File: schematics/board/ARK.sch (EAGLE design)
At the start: 207 parts, among them IC2 STM32F103C8T, Q5 8MHz

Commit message: Резисторы у FS8205A 100Ом
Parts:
- R88, R89, R90, R91, R92, R93, R94, R95, R96, R97, R98, R99: value 10k -> 100R
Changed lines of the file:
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@@
 <part name="R62" library="resistor" library_urn="urn:adsk.eagle:library:348" deviceset="R-US_" device="R0603" package3d_urn="urn:adsk.eagle:package:23555/3" value="232k"/>
 <part name="R87" library="resistor" library_urn="urn:adsk.eagle:library:348" deviceset="R-US_" device="R0603" package3d_urn="urn:adsk.eagle:package:23555/3" value="680k"/>
-<part name="R88" library="resistor" library_urn="urn:adsk.eagle:library:348" deviceset="R-US_" device="R0603" package3d_urn="urn:adsk.eagle:package:23555/3" value="10k"/>
-<part name="R89" library="resistor" library_urn="urn:adsk.eagle:library:348" deviceset="R-US_" device="R0603" package3d_urn="urn:adsk.eagle:package:23555/3" value="10k"/>
-<part name="R90" library="resistor" library_urn="urn:adsk.eagle:library:348" deviceset="R-US_" device="R0603" package3d_urn="urn:adsk.eagle:package:23555/3" value="10k"/>
-<part name="R91" library="resistor" library_urn="urn:adsk.eagle:library:348" deviceset="R-US_" device="R0603" package3d_urn="urn:adsk.eagle:package:23555/3" value="10k"/>
-<part name="R92" library="resistor" library_urn="urn:adsk.eagle:library:348" deviceset="R-US_" device="R0603" package3d_urn="urn:adsk.eagle:package:23555/3" value="10k"/>
-<part name="R93" library="resistor" library_urn="urn:adsk.eagle:library:348" deviceset="R-US_" device="R0603" package3d_urn="urn:adsk.eagle:package:23555/3" value="10k"/>
-<part name="R94" library="resistor" library_urn="urn:adsk.eagle:library:348" deviceset="R-US_" device="R0603" package3d_urn="urn:adsk.eagle:package:23555/3" value="10k"/>
-<part name="R95" library="resistor" library_urn="urn:adsk.eagle:library:348" deviceset="R-US_" device="R0603" package3d_urn="urn:adsk.eagle:package:23555/3" value="10k"/>
-<part name="R96" library="resistor" library_urn="urn:adsk.eagle:library:348" deviceset="R-US_" device="R0603" package3d_urn="urn:adsk.eagle:package:23555/3" value="10k"/>
-<part name="R97" library="resistor" library_urn="urn:adsk.eagle:library:348" deviceset="R-US_" device="R0603" package3d_urn="urn:adsk.eagle:package:23555/3" value="10k"/>
-<part name="R98" library="resistor" library_urn="urn:adsk.eagle:library:348" deviceset="R-US_" device="R0603" package3d_urn="urn:adsk.eagle:package:23555/3" value="10k"/>
-<part name="R99" library="resistor" library_urn="urn:adsk.eagle:library:348" deviceset="R-US_" device="R0603" package3d_urn="urn:adsk.eagle:package:23555/3" value="10k"/>
+<part name="R88" library="resistor" library_urn="urn:adsk.eagle:library:348" deviceset="R-US_" device="R0603" package3d_urn="urn:adsk.eagle:package:23555/3" value="100R"/>
+<part name="R89" library="resistor" library_urn="urn:adsk.eagle:library:348" deviceset="R-US_" device="R0603" package3d_urn="urn:adsk.eagle:package:23555/3" value="100R"/>
+<part name="R90" library="resistor" library_urn="urn:adsk.eagle:library:348" deviceset="R-US_" device="R0603" package3d_urn="urn:adsk.eagle:package:23555/3" value="100R"/>
+<part name="R91" library="resistor" library_urn="urn:adsk.eagle:library:348" deviceset="R-US_" device="R0603" package3d_urn="urn:adsk.eagle:package:23555/3" value="100R"/>
+<part name="R92" library="resistor" library_urn="urn:adsk.eagle:library:348" deviceset="R-US_" device="R0603" package3d_urn="urn:adsk.eagle:package:23555/3" value="100R"/>
+<part name="R93" library="resistor" library_urn="urn:adsk.eagle:library:348" deviceset="R-US_" device="R0603" package3d_urn="urn:adsk.eagle:package:23555/3" value="100R"/>
+<part name="R94" library="resistor" library_urn="urn:adsk.eagle:library:348" deviceset="R-US_" device="R0603" package3d_urn="urn:adsk.eagle:package:23555/3" value="100R"/>
+<part name="R95" library="resistor" library_urn="urn:adsk.eagle:library:348" deviceset="R-US_" device="R0603" package3d_urn="urn:adsk.eagle:package:23555/3" value="100R"/>
+<part name="R96" library="resistor" library_urn="urn:adsk.eagle:library:348" deviceset="R-US_" device="R0603" package3d_urn="urn:adsk.eagle:package:23555/3" value="100R"/>
+<part name="R97" library="resistor" library_urn="urn:adsk.eagle:library:348" deviceset="R-US_" device="R0603" package3d_urn="urn:adsk.eagle:package:23555/3" value="100R"/>
+<part name="R98" library="resistor" library_urn="urn:adsk.eagle:library:348" deviceset="R-US_" device="R0603" package3d_urn="urn:adsk.eagle:package:23555/3" value="100R"/>
+<part name="R99" library="resistor" library_urn="urn:adsk.eagle:library:348" deviceset="R-US_" device="R0603" package3d_urn="urn:adsk.eagle:package:23555/3" value="100R"/>
 <part name="PWR" library="led" library_urn="urn:adsk.eagle:library:259" deviceset="LED" device="CHIPLED_0603" package3d_urn="urn:adsk.eagle:package:15822/2"/>
 <part name="PB5" library="led" library_urn="urn:adsk.eagle:library:259" deviceset="LED" device="CHIPLED_0603" package3d_urn="urn:adsk.eagle:package:15822/2"/>

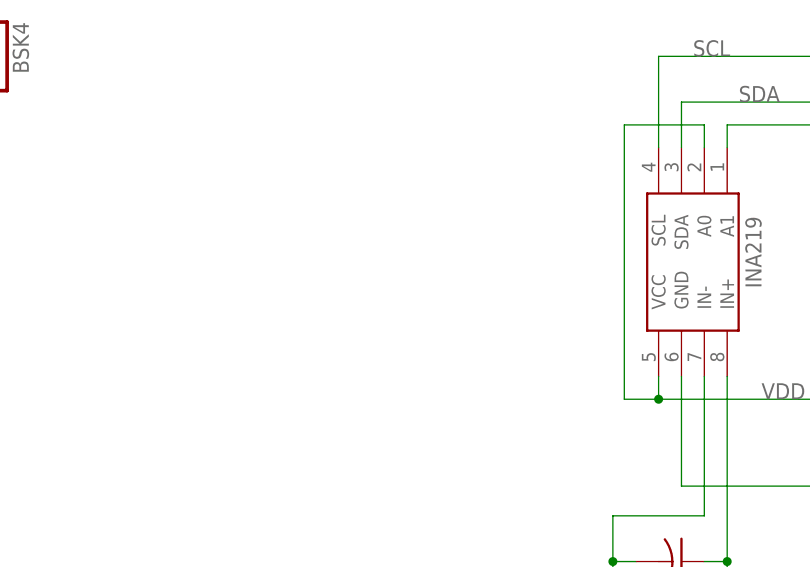
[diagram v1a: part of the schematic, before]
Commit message: Добавлен micro-USB на АРК
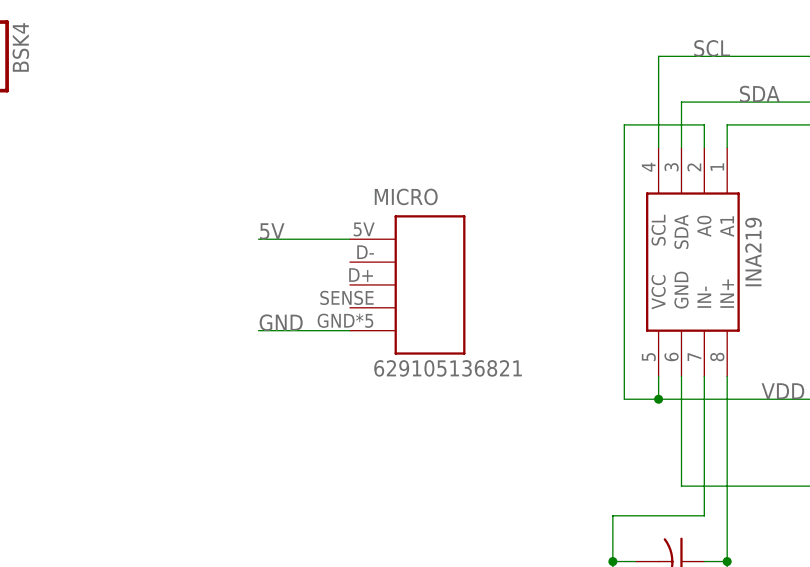
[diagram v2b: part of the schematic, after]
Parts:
- added MICRO: 629105136821, MicroUSB:629105136821
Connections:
- net 5V: now also MICRO.1
- net GND: now also MICRO.5
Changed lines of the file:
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@@
 <layer number="48" name="Document" color="7" fill="1" visible="no" active="no"/>
 <layer number="49" name="Reference" color="7" fill="1" visible="no" active="no"/>
+<layer number="50" name="dxf" color="7" fill="1" visible="no" active="no"/>
 <layer number="51" name="tDocu" color="7" fill="1" visible="no" active="no"/>
 <layer number="52" name="bDocu" color="7" fill="1" visible="no" active="no"/>
+<layer number="53" name="tGND_GNDA" color="7" fill="9" visible="no" active="no"/>
+<layer number="54" name="bGND_GNDA" color="1" fill="9" visible="no" active="no"/>
+<layer number="56" name="wert" color="7" fill="1" visible="no" active="no"/>
 <layer number="88" name="SimResults" color="9" fill="1" visible="yes" active="yes"/>
 <layer number="89" name="SimProbes" color="9" fill="1" visible="yes" active="yes"/>
@@
 <layer number="101" name="NotChangedData" color="15" fill="1" visible="yes" active="yes"/>
 <layer number="102" name="ChangedData" color="15" fill="1" visible="yes" active="yes"/>
+<layer number="103" name="tMap" color="7" fill="1" visible="no" active="no"/>
+<layer number="104" name="Name" color="7" fill="1" visible="no" active="no"/>
+<layer number="105" name="tPlate" color="7" fill="1" visible="no" active="no"/>
+<layer number="106" name="bPlate" color="7" fill="1" visible="no" active="no"/>
+<layer number="107" name="Crop" color="7" fill="1" visible="no" active="no"/>
+<layer number="108" name="fp8" color="7" fill="1" visible="no" active="no"/>
+<layer number="109" name="fp9" color="7" fill="1" visible="no" active="no"/>
+<layer number="110" name="110" color="7" fill="1" visible="no" active="no"/>
+<layer number="111" name="111" color="7" fill="1" visible="no" active="no"/>
+<layer number="112" name="tSilk" color="7" fill="1" visible="no" active="no"/>
+<layer number="113" name="IDFDebug" color="7" fill="1" visible="no" active="yes"/>
+<layer number="116" name="Patch_BOT" color="9" fill="4" visible="no" active="no"/>
+<layer number="118" name="Rect_Pads" color="7" fill="1" visible="no" active="no"/>
+<layer number="121" name="_tsilk" color="7" fill="1" visible="no" active="no"/>
+<layer number="122" name="_bsilk" color="7" fill="1" visible="no" active="no"/>
+<layer number="123" name="tTestmark" color="7" fill="1" visible="no" active="no"/>
+<layer number="124" name="bTestmark" color="7" fill="1" visible="no" active="no"/>
+<layer number="125" name="_tNames" color="7" fill="1" visible="no" active="no"/>
+<layer number="126" name="_bNames" color="7" fill="1" visible="no" active="no"/>
+<layer number="127" name="_tValues" color="7" fill="1" visible="no" active="no"/>
+<layer number="128" name="_bValues" color="7" fill="1" visible="no" active="no"/>
+<layer number="131" name="tAdjust" color="7" fill="1" visible="no" active="no"/>
+<layer number="132" name="bAdjust" color="7" fill="1" visible="no" active="no"/>
+<layer number="144" name="DrillLegend" color="7" fill="1" visible="no" active="no"/>
+<layer number="151" name="HeatSink" color="14" fill="1" visible="no" active="no"/>
+<layer number="152" name="_bDocu" color="7" fill="1" visible="no" active="no"/>
+<layer number="199" name="Contour" color="7" fill="1" visible="no" active="no"/>
+<layer number="200" name="200bmp" color="1" fill="10" visible="no" active="no"/>
+<layer number="201" name="201bmp" color="2" fill="1" visible="no" active="no"/>
+<layer number="202" name="202bmp" color="3" fill="1" visible="no" active="no"/>
+<layer number="203" name="203bmp" color="4" fill="10" visible="no" active="no"/>
+<layer number="204" name="204bmp" color="5" fill="10" visible="no" active="no"/>
+<layer number="205" name="205bmp" color="6" fill="10" visible="no" active="no"/>
+<layer number="206" name="206bmp" color="7" fill="10" visible="no" active="no"/>
+<layer number="207" name="207bmp" color="15" fill="10" visible="no" active="no"/>
+<layer number="208" name="208bmp" color="9" fill="10" visible="no" active="no"/>
+<layer number="209" name="209bmp" color="7" fill="1" visible="no" active="no"/>
+<layer number="210" name="210bmp" color="7" fill="1" visible="no" active="no"/>
+<layer number="211" name="211bmp" color="7" fill="1" visible="no" active="no"/>
+<layer number="212" name="212bmp" color="7" fill="1" visible="no" active="no"/>
+<layer number="213" name="213bmp" color="7" fill="1" visible="no" active="no"/>
+<layer number="214" name="214bmp" color="7" fill="1" visible="no" active="no"/>
+<layer number="215" name="215bmp" color="7" fill="1" visible="no" active="no"/>
+<layer number="216" name="216bmp" color="7" fill="1" visible="no" active="no"/>
+<layer number="217" name="217bmp" color="18" fill="1" visible="no" active="no"/>
+<layer number="218" name="218bmp" color="19" fill="1" visible="no" active="no"/>
+<layer number="219" name="219bmp" color="20" fill="1" visible="no" active="no"/>
+<layer number="220" name="220bmp" color="21" fill="1" visible="no" active="no"/>
+<layer number="221" name="221bmp" color="22" fill="1" visible="no" active="no"/>
+<layer number="222" name="222bmp" color="23" fill="1" visible="no" active="no"/>
+<layer number="223" name="223bmp" color="24" fill="1" visible="no" active="no"/>
+<layer number="224" name="224bmp" color="25" fill="1" visible="no" active="no"/>
+<layer number="225" name="225bmp" color="7" fill="1" visible="no" active="yes"/>
+<layer number="226" name="226bmp" color="7" fill="1" visible="no" active="yes"/>
+<layer number="227" name="227bmp" color="7" fill="1" visible="no" active="yes"/>
+<layer number="228" name="228bmp" color="7" fill="1" visible="no" active="yes"/>
+<layer number="230" name="230bmp" color="7" fill="1" visible="no" active="yes"/>
+<layer number="248" name="Housing" color="7" fill="1" visible="no" active="no"/>
+<layer number="249" name="Edge" color="7" fill="1" visible="no" active="no"/>
+<layer number="250" name="Descript" color="7" fill="1" visible="no" active="yes"/>
+<layer number="251" name="SMDround" color="7" fill="1" visible="no" active="yes"/>
+<layer number="254" name="OrgLBR" color="13" fill="1" visible="no" active="no"/>
 </layers>
 <schematic xreflabel="%F%N/%S.%C%R" xrefpart="/%S.%C%R">
@@
 <part name="R25" library="resistor" library_urn="urn:adsk.eagle:library:348" deviceset="R-US_" device="R0603" package3d_urn="urn:adsk.eagle:package:23555/3" value="5k1"/>
 <part name="R26" library="resistor" library_urn="urn:adsk.eagle:library:348" deviceset="R-US_" device="R0603" package3d_urn="urn:adsk.eagle:package:23555/3" value="5k1"/>
+<part name="MICRO" library="MicroUSB" deviceset="629105136821" device=""/>
 </parts>
 <sheets>
@@
 <attribute name="VALUE" x="534.162" y="290.83" size="1.778" layer="96" rot="R90"/>
 </instance>
+<instance part="MICRO" gate="G$1" x="515.62" y="231.14" smashed="yes">
+<attribute name="NAME" x="508" y="245.11" size="1.778" layer="95"/>
+<attribute name="VALUE" x="508" y="226.06" size="1.778" layer="96"/>
+</instance>
 </instances>
 <busses>
@@
 <label x="513.08" y="312.42" size="1.778" layer="95" rot="R90"/>
 </segment>
+<segment>
+<pinref part="MICRO" gate="G$1" pin="5"/>
+<wire x1="505.46" y1="231.14" x2="495.3" y2="231.14" width="0.1524" layer="91"/>
+<label x="495.3" y="231.14" size="1.778" layer="95"/>
+</segment>
 </net>
 <net name="INA_BUS+" class="0">
@@
 <pinref part="BSK4" gate="A" pin="8"/>
 </segment>
+<segment>
+<pinref part="MICRO" gate="G$1" pin="1"/>
+<wire x1="505.46" y1="241.3" x2="495.3" y2="241.3" width="0.1524" layer="91"/>
+<label x="495.3" y="241.3" size="1.778" layer="95"/>
+</segment>
 </net>

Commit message: Изменения в подключении мк
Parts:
- added C15, C53, C54, C55: 100nF, rcl:C-EUC0603
- added C16: 10µ, rcl:C-USC1206
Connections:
- net GND: now also C15.2, C16.2, C53.2, C54.2, C55.2
- net VDD: now also C15.1, C16.1, C53.1, C54.1, C55.1, IC2.VBAT
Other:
- moved on the sheet: R79
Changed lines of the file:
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@@
 <part name="R26" library="resistor" library_urn="urn:adsk.eagle:library:348" deviceset="R-US_" device="R0603" package3d_urn="urn:adsk.eagle:package:23555/3" value="5k1"/>
 <part name="MICRO" library="MicroUSB" deviceset="629105136821" device=""/>
+<part name="C15" library="rcl" library_urn="urn:adsk.eagle:library:334" deviceset="C-EU" device="C0603" package3d_urn="urn:adsk.eagle:package:23616/2" value="100nF"/>
+<part name="C16" library="rcl" library_urn="urn:adsk.eagle:library:334" deviceset="C-US" device="C1206" package3d_urn="urn:adsk.eagle:package:23618/2" value="10µ"/>
+<part name="C53" library="rcl" library_urn="urn:adsk.eagle:library:334" deviceset="C-EU" device="C0603" package3d_urn="urn:adsk.eagle:package:23616/2" value="100nF"/>
+<part name="C54" library="rcl" library_urn="urn:adsk.eagle:library:334" deviceset="C-EU" device="C0603" package3d_urn="urn:adsk.eagle:package:23616/2" value="100nF"/>
+<part name="C55" library="rcl" library_urn="urn:adsk.eagle:library:334" deviceset="C-EU" device="C0603" package3d_urn="urn:adsk.eagle:package:23616/2" value="100nF"/>
 </parts>
 <sheets>
@@
 <instance part="U$26" gate="G$1" x="58.42" y="43.18" smashed="yes"/>
 <instance part="U$1" gate="G$1" x="241.3" y="50.8" smashed="yes"/>
-<instance part="R79" gate="G$1" x="462.28" y="378.46" smashed="yes">
-<attribute name="NAME" x="458.47" y="379.9586" size="1.778" layer="95"/>
-<attribute name="VALUE" x="458.47" y="375.158" size="1.778" layer="96"/>
+<instance part="R79" gate="G$1" x="441.96" y="375.92" smashed="yes">
+<attribute name="NAME" x="438.15" y="377.4186" size="1.778" layer="95"/>
+<attribute name="VALUE" x="438.15" y="372.618" size="1.778" layer="96"/>
 </instance>
 <instance part="LED3" gate="G$1" x="297.18" y="292.1" smashed="yes" rot="R270">
@@
 <attribute name="VALUE" x="508" y="226.06" size="1.778" layer="96"/>
 </instance>
+<instance part="C15" gate="G$1" x="472.44" y="383.54" smashed="yes" rot="R270">
+<attribute name="NAME" x="472.821" y="382.016" size="1.778" layer="95" rot="R270"/>
+<attribute name="VALUE" x="467.741" y="382.016" size="1.778" layer="96" rot="R270"/>
+</instance>
+<instance part="C16" gate="G$1" x="472.44" y="388.62" smashed="yes" rot="R270">
+<attribute name="NAME" x="473.075" y="387.604" size="1.778" layer="95" rot="R270"/>
+<attribute name="VALUE" x="468.249" y="387.604" size="1.778" layer="96" rot="R270"/>
+</instance>
+<instance part="C53" gate="G$1" x="472.44" y="396.24" smashed="yes" rot="R270">
+<attribute name="NAME" x="472.821" y="394.716" size="1.778" layer="95" rot="R270"/>
+<attribute name="VALUE" x="467.741" y="394.716" size="1.778" layer="96" rot="R270"/>
+</instance>
+<instance part="C54" gate="G$1" x="472.44" y="403.86" smashed="yes" rot="R270">
+<attribute name="NAME" x="472.821" y="402.336" size="1.778" layer="95" rot="R270"/>
+<attribute name="VALUE" x="467.741" y="402.336" size="1.778" layer="96" rot="R270"/>
+</instance>
+<instance part="C55" gate="G$1" x="472.44" y="411.48" smashed="yes" rot="R270">
+<attribute name="NAME" x="472.821" y="409.956" size="1.778" layer="95" rot="R270"/>
+<attribute name="VALUE" x="467.741" y="409.956" size="1.778" layer="96" rot="R270"/>
+</instance>
 </instances>
 <busses>
@@
 </segment>
 <segment>
-<wire x1="472.44" y1="368.3" x2="472.44" y2="375.92" width="0.1524" layer="91"/>
-<label x="472.44" y="370.84" size="1.778" layer="95" rot="R90"/>
+<wire x1="472.44" y1="368.3" x2="472.44" y2="378.46" width="0.1524" layer="91"/>
+<label x="467.36" y="424.18" size="1.778" layer="95" rot="R90"/>
 <pinref part="IC2" gate="MCU" pin="VSSA"/>
+<wire x1="472.44" y1="378.46" x2="467.36" y2="378.46" width="0.1524" layer="91"/>
+<wire x1="467.36" y1="378.46" x2="467.36" y2="383.54" width="0.1524" layer="91"/>
+<pinref part="C15" gate="G$1" pin="2"/>
+<wire x1="467.36" y1="383.54" x2="467.36" y2="388.62" width="0.1524" layer="91"/>
+<junction x="467.36" y="383.54"/>
+<pinref part="C16" gate="G$1" pin="2"/>
+<wire x1="467.36" y1="388.62" x2="467.36" y2="396.24" width="0.1524" layer="91"/>
+<junction x="467.36" y="388.62"/>
+<pinref part="C53" gate="G$1" pin="2"/>
+<wire x1="467.36" y1="396.24" x2="467.36" y2="403.86" width="0.1524" layer="91"/>
+<junction x="467.36" y="396.24"/>
+<pinref part="C54" gate="G$1" pin="2"/>
+<wire x1="467.36" y1="403.86" x2="467.36" y2="411.48" width="0.1524" layer="91"/>
+<junction x="467.36" y="403.86"/>
+<pinref part="C55" gate="G$1" pin="2"/>
+<wire x1="467.36" y1="411.48" x2="467.36" y2="429.26" width="0.1524" layer="91"/>
+<junction x="467.36" y="411.48"/>
 </segment>
 <segment>
@@
 </segment>
 <segment>
-<wire x1="474.98" y1="368.3" x2="474.98" y2="375.92" width="0.1524" layer="91"/>
-<label x="474.98" y="370.84" size="1.778" layer="95" rot="R90"/>
+<wire x1="474.98" y1="368.3" x2="474.98" y2="383.54" width="0.1524" layer="91"/>
+<label x="474.98" y="424.18" size="1.778" layer="95" rot="R90"/>
 <pinref part="IC2" gate="MCU" pin="VDDA"/>
+<pinref part="C15" gate="G$1" pin="1"/>
+<wire x1="474.98" y1="383.54" x2="474.98" y2="388.62" width="0.1524" layer="91"/>
+<junction x="474.98" y="383.54"/>
+<pinref part="C16" gate="G$1" pin="1"/>
+<wire x1="474.98" y1="388.62" x2="474.98" y2="396.24" width="0.1524" layer="91"/>
+<junction x="474.98" y="388.62"/>
+<pinref part="C53" gate="G$1" pin="1"/>
+<wire x1="474.98" y1="396.24" x2="474.98" y2="403.86" width="0.1524" layer="91"/>
+<junction x="474.98" y="396.24"/>
+<pinref part="C54" gate="G$1" pin="1"/>
+<wire x1="474.98" y1="403.86" x2="474.98" y2="411.48" width="0.1524" layer="91"/>
+<junction x="474.98" y="403.86"/>
+<pinref part="C55" gate="G$1" pin="1"/>
+<wire x1="474.98" y1="411.48" x2="474.98" y2="429.26" width="0.1524" layer="91"/>
+<junction x="474.98" y="411.48"/>
+<pinref part="IC2" gate="MCU" pin="VBAT"/>
+<wire x1="477.52" y1="368.3" x2="474.98" y2="368.3" width="0.1524" layer="91"/>
+<junction x="474.98" y="368.3"/>
 </segment>
 <segment>
@@
 </segment>
 <segment>
-<wire x1="457.2" y1="378.46" x2="447.04" y2="378.46" width="0.1524" layer="91"/>
-<label x="454.66" y="378.46" size="1.778" layer="95" rot="R180"/>
+<wire x1="436.88" y1="375.92" x2="426.72" y2="375.92" width="0.1524" layer="91"/>
+<label x="434.34" y="375.92" size="1.778" layer="95" rot="R180"/>
 <pinref part="R79" gate="G$1" pin="1"/>
 </segment>
@@
 <net name="NRST" class="0">
 <segment>
-<wire x1="467.36" y1="368.3" x2="467.36" y2="378.46" width="0.1524" layer="91"/>
 <pinref part="R79" gate="G$1" pin="2"/>
-<wire x1="467.36" y1="378.46" x2="467.36" y2="393.7" width="0.1524" layer="91"/>
-<junction x="467.36" y="378.46"/>
-<label x="467.36" y="386.08" size="1.778" layer="95" rot="R90"/>
+<wire x1="447.04" y1="375.92" x2="447.04" y2="391.16" width="0.1524" layer="91"/>
+<label x="447.04" y="383.54" size="1.778" layer="95" rot="R90"/>
 <pinref part="IC2" gate="MCU" pin="NRST"/>
+<wire x1="447.04" y1="375.92" x2="467.36" y2="375.92" width="0.1524" layer="91"/>
+<wire x1="467.36" y1="375.92" x2="467.36" y2="368.3" width="0.1524" layer="91"/>
+<junction x="447.04" y="375.92"/>
 </segment>
 <segment>
